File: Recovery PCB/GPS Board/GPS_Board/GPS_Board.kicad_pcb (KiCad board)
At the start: 2 copper layers, 85.7 x 50.8 mm, 23 parts, among them J1 XT30-M, J2 XT30-M, U1 Teensy4.1, U2 D24V22F5_VoltageRegulator, U3 LD1117v33, U4 conn_recovery10, U5 conn_recovery10, U6 conn_recovery8

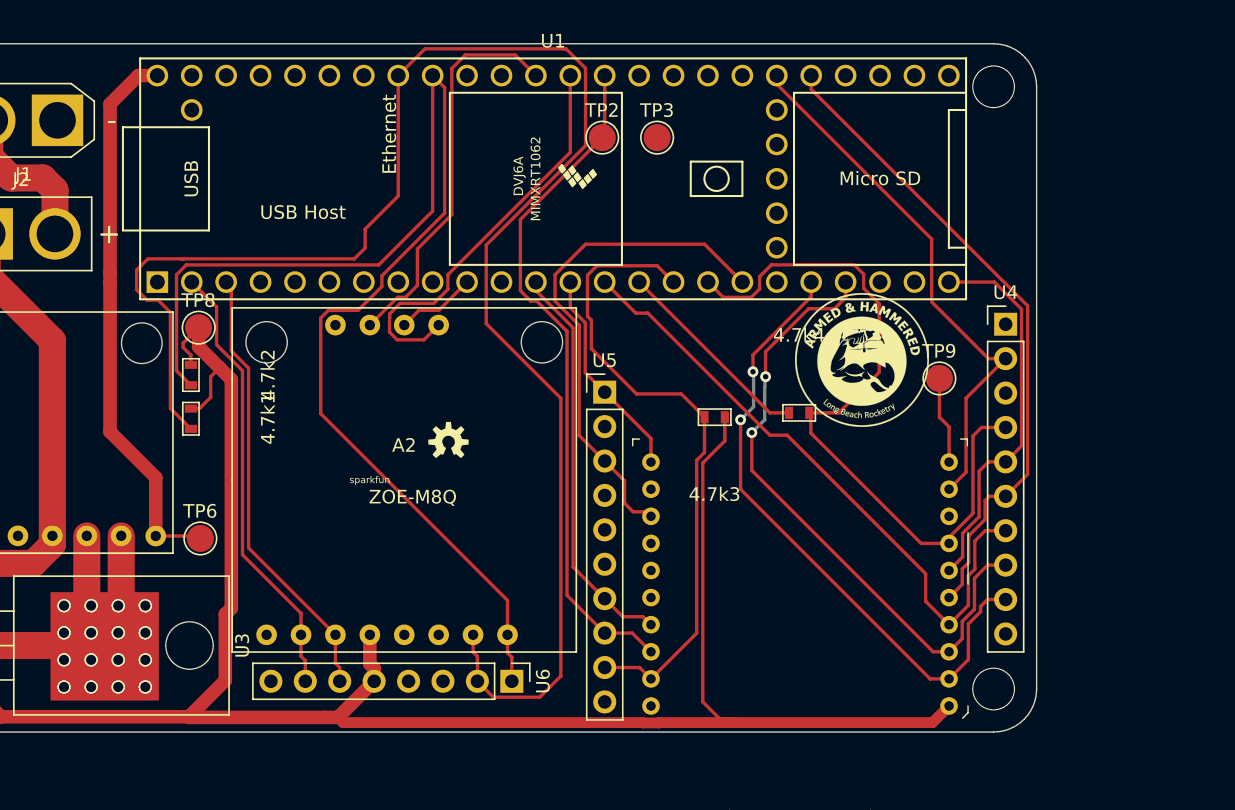
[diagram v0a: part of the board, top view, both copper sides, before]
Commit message: Added teensy breakout pads
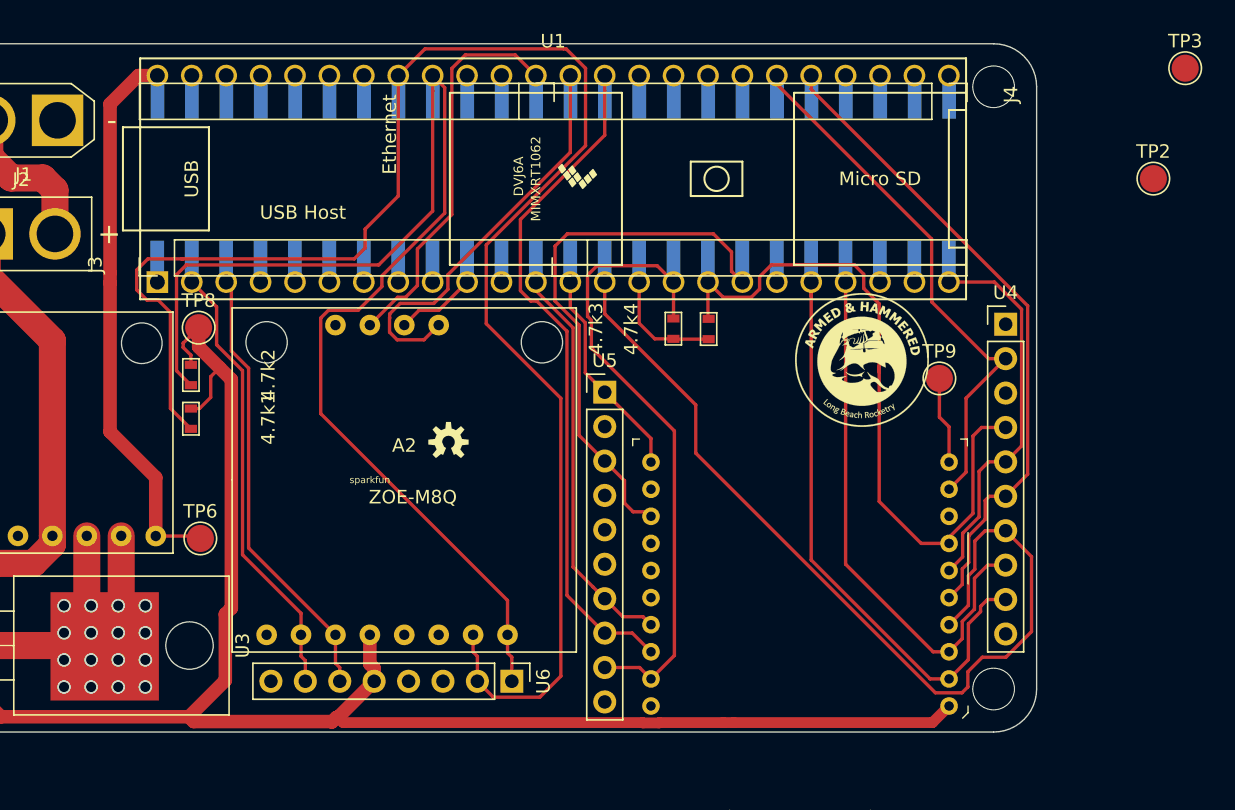
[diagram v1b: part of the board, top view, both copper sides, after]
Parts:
- added J3: Conn_01x24_Male, GPS Board:SMD_Connector_1x24, F.Cu at (131.9, 76.1)
- added J4: Conn_01x24_Male, GPS Board:SMD_Connector_1x24, F.Cu at (190.4, 64.6)
- moved TP2 40.8 mm to (205.5, 70.3)
- moved TP3 39.3 mm to (207.8, 62.1)
- moved 4.7k4 9.11 mm to (172.6, 81.4), turned to 90 degrees
- moved 4.7k3 7.21 mm to (170.0, 81.4), turned to 90 degrees
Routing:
- net +3V3: track 165.4 -> 137.0 mm
- net /XBEE_MISO: track 46.6 -> 69.6 mm
- net GND: track 51.4 -> 57.1 mm
- net /XBEE_RX: track 46.9 -> 41.8 mm, vias 2 -> 0
- net /XBEE_SLEEP: track 37.3 -> 41.7 mm
- net /GPS_INT: track 30.2 -> 33.7 mm
- net Net-(J4-Pad8): track 0.00 -> 1.91 mm
- net Net-(J4-Pad4): track 0.00 -> 1.91 mm
- net Net-(J4-Pad22): track 0.00 -> 1.91 mm
- net Net-(J4-Pad19): track 0.00 -> 1.91 mm
- net Net-(J4-Pad15): track 0.00 -> 1.91 mm
- net Net-(J4-Pad1): track 0.00 -> 1.91 mm
- net /XBEE_SCK: track 50.5 -> 52.5 mm
- net /XBEE_RESET: track 48.3 -> 50.2 mm
- net /XBEE_DTR: track 40.0 -> 41.9 mm
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
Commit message: Added Silkscreen doge
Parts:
- added G***: LOGO, GPS Board:doge_recovery, B.Cu at (148.4, 87.5)

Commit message: Moved 3.3v Trace
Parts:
- moved TP3 42.9 mm to (172.6, 86.7)
- moved G*** 36.7 mm to (213.7, 105.1)
- moved TP2 11.8 mm to (217.0, 72.7)
- moved TP9 1.81 mm to (189.0, 86.7)
- moved 4.7k2 1.75 mm to (135.5, 86.1), turned to 180 degrees
- moved 4.7k1 1.30 mm to (135.5, 88.7), turned to 180 degrees
- moved TP8 1.08 mm to (135.1, 82.4)
- moved TP5 0.60 mm to (113.1, 74.3)
- moved U6 0.28 mm to (157.8, 107.4)
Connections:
- J4 pad 22: Net-(J4-Pad22) -> +3V3
- U1 pad 46: Net-(J4-Pad22) -> +3V3
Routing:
- net +3V3: track 137.0 -> 146.2 mm
- net /XBEE_SCL: track 49.2 -> 54.4 mm
- net /XBEE_SDA: track 53.8 -> 57.9 mm
- net /XBEE_RESET: track 50.2 -> 53.7 mm
- net /XBEE_DTR: track 41.9 -> 45.2 mm
- net GND: track 57.1 -> 59.1 mm
- net Net-(J4-Pad22): track 1.91 -> 0.00 mm
- net /XBEE_TX: track 45.6 -> 44.1 mm
- net +5V: track 42.9 -> 43.5 mm
- net /XBEE_MOSI: track 17.5 -> 18.1 mm
- net /XBEE_SLEEP: track 41.7 -> 42.3 mm
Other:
- rule trace_min: 0.2 -> 0.15
- board text added: "Created By: - Alejandro Martinez - Allan Flores - Brianna Clark - Joey Otanez - Jojo Navasca"

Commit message: Removed testpoint
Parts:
- removed TP2: TestPoint, TestPoint:TestPoint_Pad_D2.0mm
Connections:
- J3 pad 15: +3V3 -> Net-(J3-Pad15)
- U1 pad 15: +3V3 -> Net-(J3-Pad15)
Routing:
- net Net-(J3-Pad15): track 0.00 -> 3.67 mm
- net +3V3: track 146.2 -> 144.4 mm

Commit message: Added 0 ohm resistors
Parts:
- added ?: , , F.Cu at (121.3, 88.1)
- added ?: , , F.Cu at (121.9, 88.3)
- added ?: , , F.Cu at (141.6, 72.7)
- added ?: , , F.Cu at (141.4, 72.8)
- G***: moved to B.Cu
- moved G*** 32.7 mm to (188.1, 84.7), turned to 270 degrees
- renumbered 4.7k4 to 4.7k, 4.7k3 to 4.7k
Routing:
- net /XBEE_TX: track 44.1 -> 24.2 mm
- added copper zone on B.Cu, net GND
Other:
- board text added: "GPS"
- board text added: "KEY"
- board text added: "REGULATOR"
- board text added: "TEENSY"
- board text added: "XBEE"

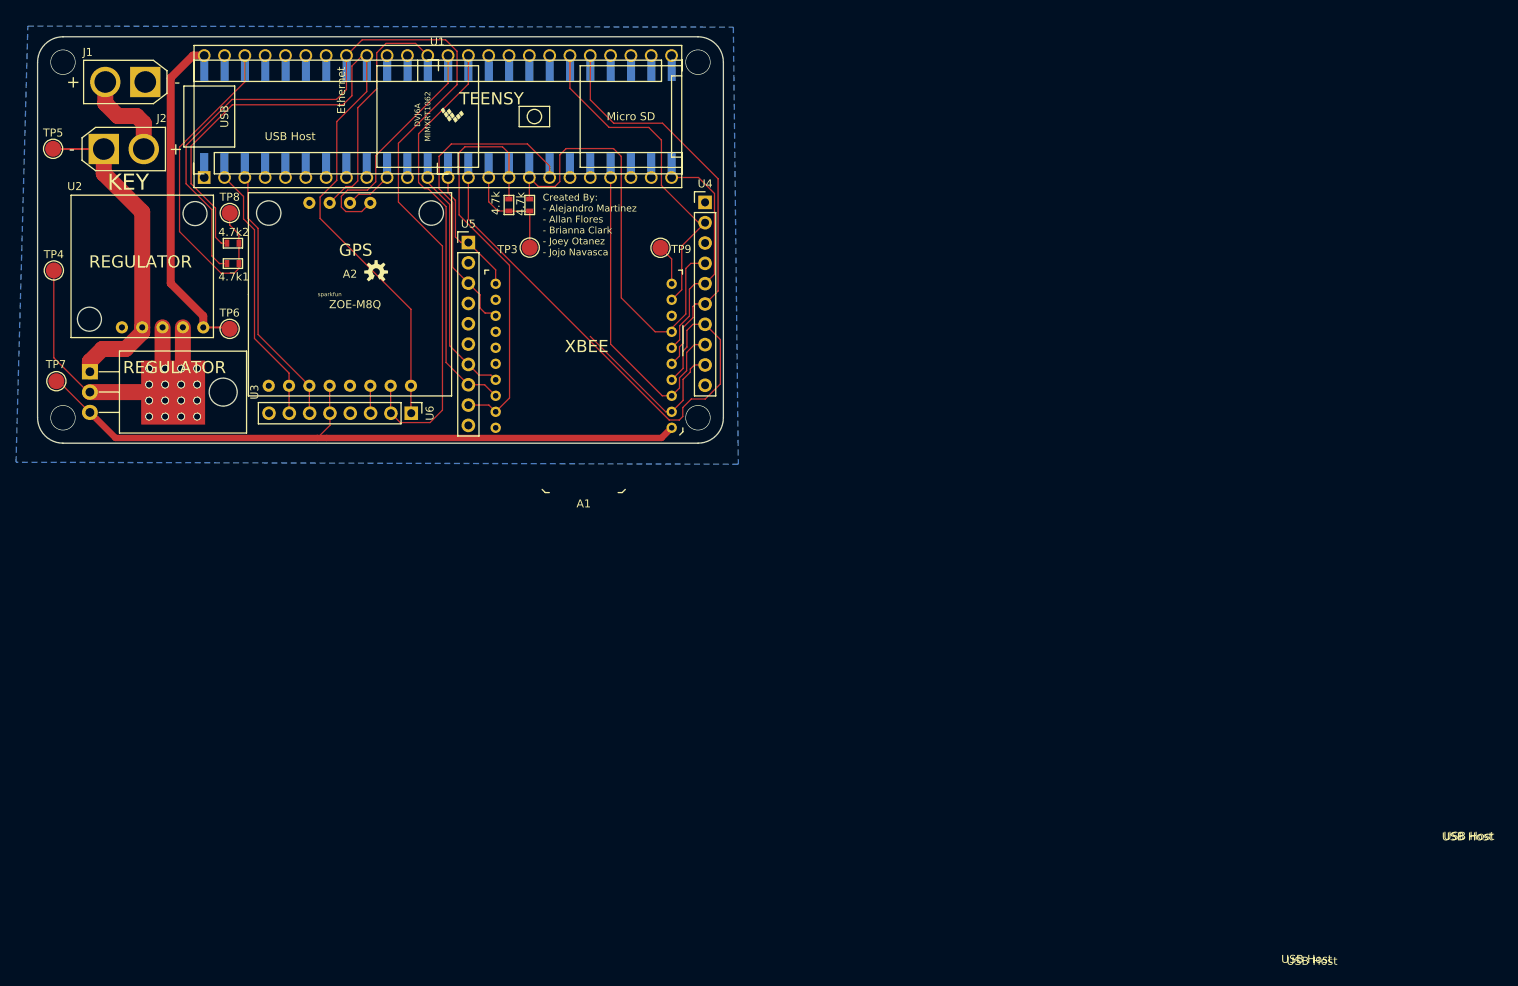
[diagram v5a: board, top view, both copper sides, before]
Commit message: Added 0 ohm resistors on backside
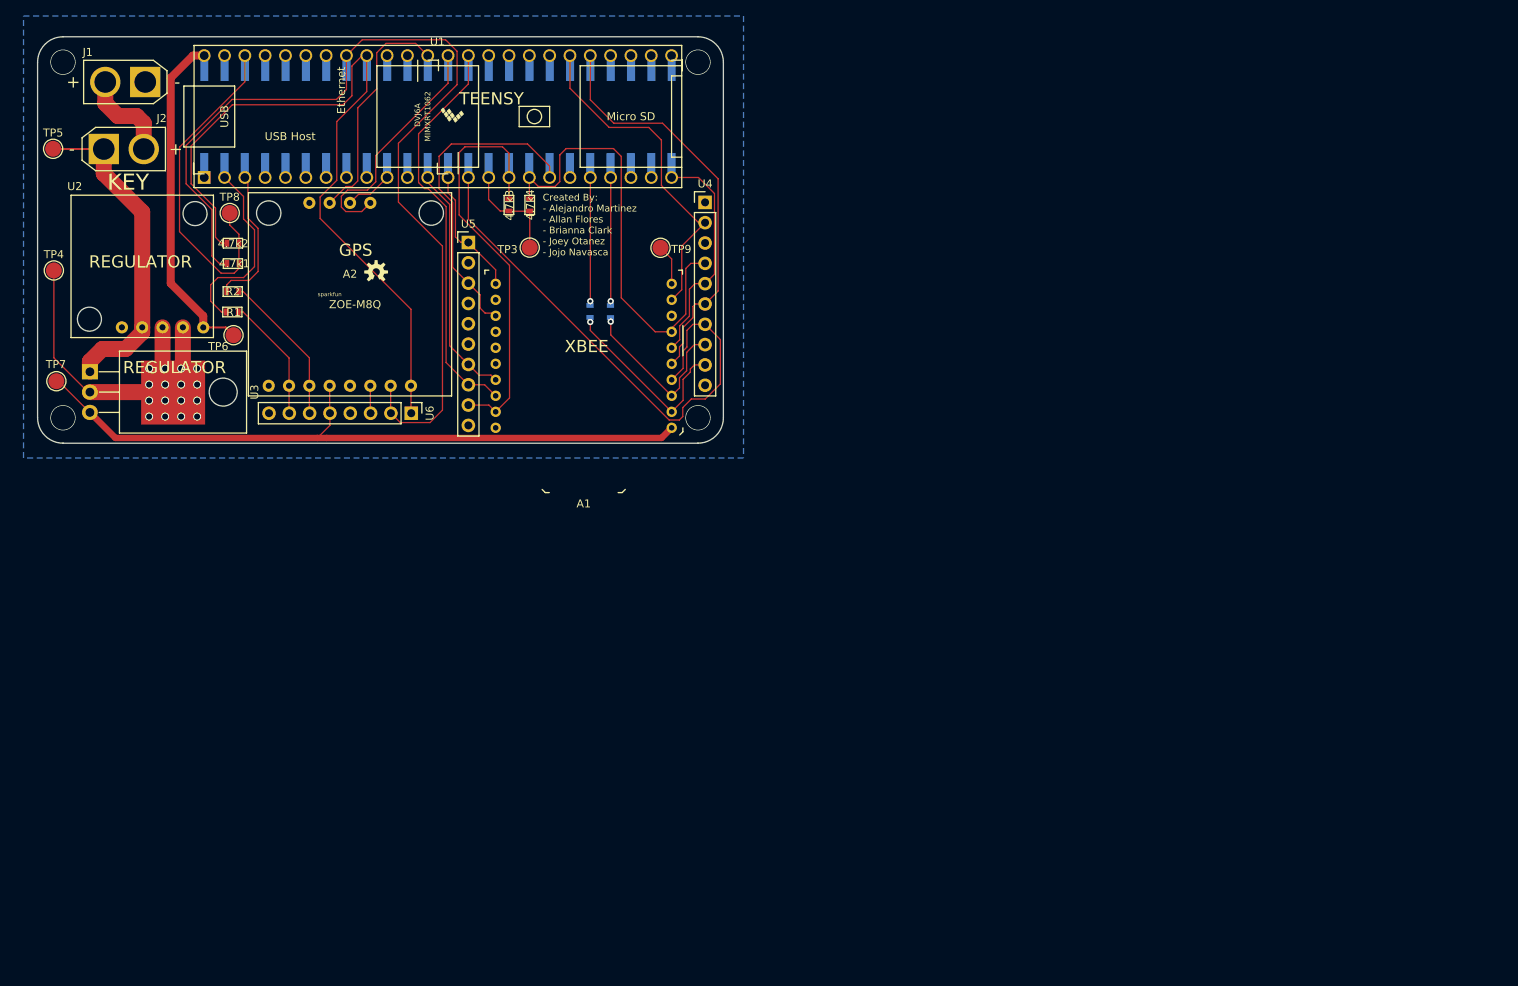
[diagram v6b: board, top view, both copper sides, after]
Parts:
- added R1: 0, GPS Board:0603, F.Cu at (135.5, 94.7)
- added R2: 0, GPS Board:0603, F.Cu at (135.5, 92.2)
- added R3: 0, GPS Board:0603_BACK, F.Cu at (180.2, 94.7)
- added R4: 0, GPS Board:0603_BACK, F.Cu at (182.7, 94.7)
- moved TP6 0.93 mm to (135.6, 97.6)
- renumbered 4.7k to 4.7k3, 4.7k to 4.7k4
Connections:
- J3 pad 15: Net-(J3-Pad15) -> +3V3
- U1 pad 15: Net-(J3-Pad15) -> +3V3
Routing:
- net /XBEE_TX: track 24.2 -> 42.2 mm, vias 0 -> 2
- net /GPS_TX: track 34.6 -> 41.1 mm
- net /GPS_RX: track 34.6 -> 38.9 mm
- net Net-(J3-Pad15): track 3.67 -> 0.00 mm
- net /XBEE_RX: track 41.8 -> 39.7 mm, vias 0 -> 2
- net +3V3: track 144.4 -> 146.1 mm
- net +5V: track 43.5 -> 44.6 mm
